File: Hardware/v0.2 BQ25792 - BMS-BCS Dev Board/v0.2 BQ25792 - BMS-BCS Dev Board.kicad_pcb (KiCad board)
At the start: 2 copper layers, 83.4 x 30 mm, 45 parts, among them J1 Barrel Jack, J2 Barrel Jack, J3 Power Out, J5 I2C Interface, Q1 ACFET1, Q2 RBFET1, Q3 ACFET2, Q4 RBFET2, Q5 BATFET, U1 BQ25792RQMR

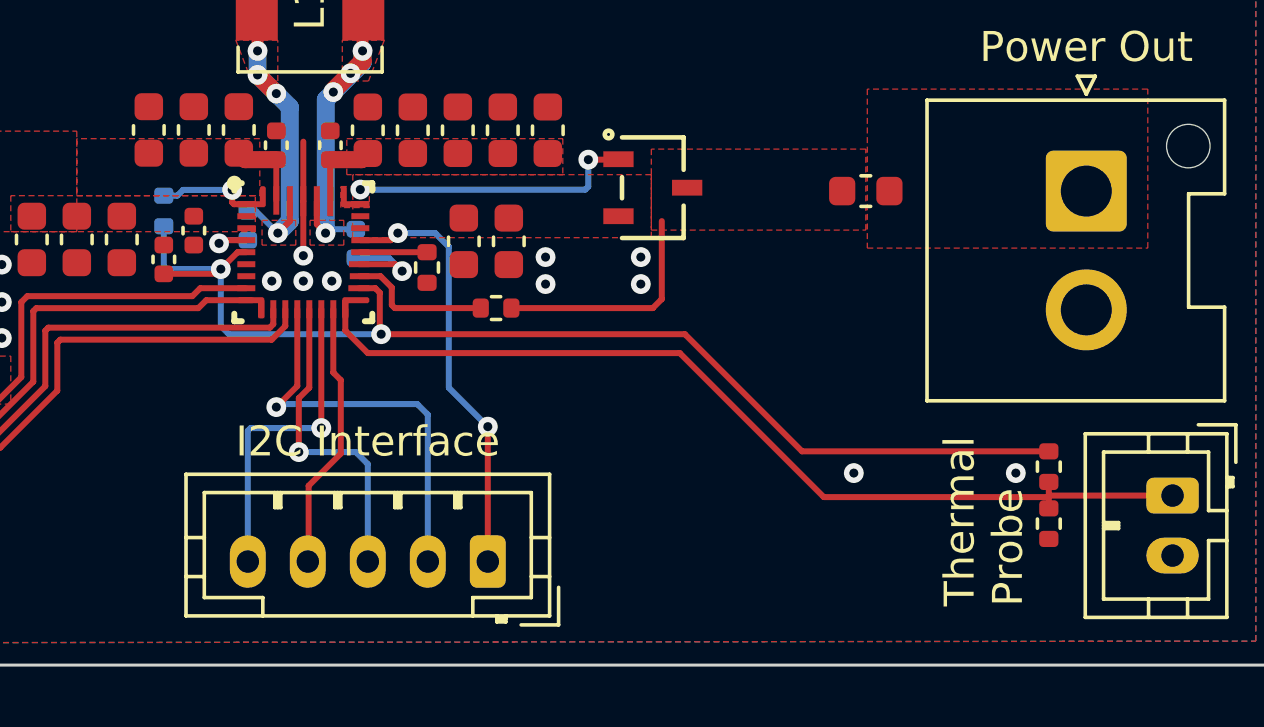
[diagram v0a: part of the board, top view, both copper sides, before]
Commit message: BMS/BCS Ordering Preparations
Finished all ordering preparations, PCB in production.
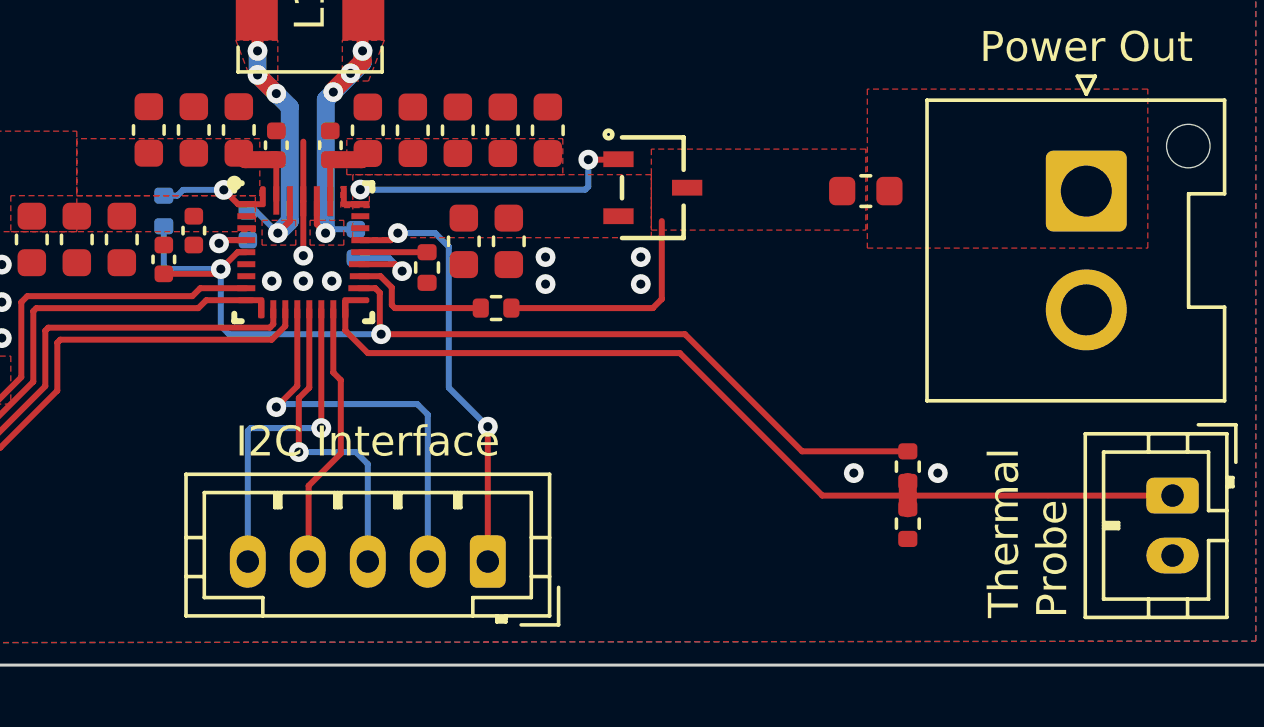
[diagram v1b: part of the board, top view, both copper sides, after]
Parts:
- moved R4 4.70 mm to (169.8, 121.8)
- moved R5 4.70 mm to (169.8, 123.7)
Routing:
- net /REGN: track 39.7 -> 35.0 mm
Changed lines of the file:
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@@
 	(footprint "Resistor_SMD:R_0402_1005Metric"
 		(layer "F.Cu")
-		(at 174.5 123.685 -90)
+		(at 169.8 123.685 -90)
 		(descr "Resistor SMD 0402 (1005 Metric), square (rectangular) end terminal, IPC_7351 nominal, (Body size source: IPC-SM-782 page 72, https://www.pcb-3d.com/wordpress/wp-content/uploads/ipc-sm-782a_amendment_1_and_2.pdf), generated with kicad-footprint-generator")
 		(tags "resistor")
@@
 	(footprint "Resistor_SMD:R_0402_1005Metric"
 		(layer "F.Cu")
-		(at 174.5 121.785 -90)
+		(at 169.8 121.785 -90)
 		(descr "Resistor SMD 0402 (1005 Metric), square (rectangular) end terminal, IPC_7351 nominal, (Body size source: IPC-SM-782 page 72, https://www.pcb-3d.com/wordpress/wp-content/uploads/ipc-sm-782a_amendment_1_and_2.pdf), generated with kicad-footprint-generator")
 		(tags "resistor")
@@
 	)
 	(gr_text "Thermal\nProbe"
-		(at 173.725 126.442858 90)
+		(at 175.2 126.831882 90)
 		(layer "F.SilkS")
 		(effects
@@
 	)
 	(via
-		(at 173.4 122)
+		(at 170.8 122)
 		(size 0.66)
 		(drill 0.3)
@@
 	)
 	(segment
-		(start 162.37 117.37)
-		(end 166.275 121.275)
+		(start 166.275 121.275)
+		(end 169.8 121.275)
 		(width 0.2)
 		(layer "F.Cu")
@@
 	)
 	(segment
-		(start 166.275 121.275)
-		(end 174.5 121.275)
+		(start 152.245478 117.37)
+		(end 162.37 117.37)
 		(width 0.2)
 		(layer "F.Cu")
@@
 	)
 	(segment
-		(start 152.049998 115.8375)
-		(end 151.499998 115.8375)
+		(start 162.37 117.37)
+		(end 166.275 121.275)
 		(width 0.2)
 		(layer "F.Cu")
@@
 	)
 	(segment
-		(start 152.2 115.987502)
-		(end 152.049998 115.8375)
+		(start 152.049998 115.8375)
+		(end 151.499998 115.8375)
 		(width 0.2)
 		(layer "F.Cu")
@@
 	)
 	(segment
-		(start 152.245478 117.37)
-		(end 162.37 117.37)
+		(start 152.2 115.987502)
+		(end 152.049998 115.8375)
 		(width 0.2)
 		(layer "F.Cu")
@@
 	)
 	(segment
-		(start 167 122.8)
-		(end 174.5 122.8)
-		(width 0.2)
-		(layer "F.Cu")
-		(net 30)
-	)
-	(segment
-		(start 162.2 118)
-		(end 167 122.8)
-		(width 0.2)
+		(start 169.8 122.295)
+		(end 169.8 122.745)
+		(width 0.6)
 		(layer "F.Cu")
 		(net 30)
 	)
 	(segment
-		(start 174.5 122.745)
-		(end 174.505 122.75)
-		(width 0.2)
+		(start 169.8 122.745)
+		(end 169.8 123.175)
+		(width 0.6)
 		(layer "F.Cu")
 		(net 30)
 	)
 	(segment
-		(start 151.049999 116.5375)
-		(end 151.049999 117.249999)
+		(start 174.505 122.75)
+		(end 178.625 122.75)
 		(width 0.2)
 		(layer "F.Cu")
@@
 	)
 	(segment
-		(start 174.5 122.295)
-		(end 174.5 122.745)
+		(start 166.945 122.75)
+		(end 174.445 122.75)
 		(width 0.2)
 		(layer "F.Cu")
@@
 	)
 	(segment
-		(start 151.049999 117.249999)
-		(end 151.8 118)
+		(start 151.049999 116.5375)
+		(end 151.049999 117.249999)
 		(width 0.2)
 		(layer "F.Cu")
@@
 	)
 	(segment
-		(start 174.5 122.745)
-		(end 174.5 123.175)
+		(start 162.2 118)
+		(end 166.945 122.745)
 		(width 0.2)
 		(layer "F.Cu")
@@
 	)
 	(segment
-		(start 174.505 122.75)
-		(end 178.625 122.75)
+		(start 151.049999 117.249999)
+		(end 151.8 118)
 		(width 0.2)
 		(layer "F.Cu")
@@
 	)
 	(segment
-		(start 147.280134 112.56047)
-		(end 147.280134 112.980134)
-		(width 0.2)
-		(layer "F.Cu")
-		(net 32)
-	)
-	(segment
-		(start 147.280134 112.980134)
-		(end 147.3375 113.0375)
+		(start 147.47703 113.0375)
+		(end 147.749999 113.0375)
 		(width 0.2)
 		(layer "F.Cu")
@@
 	)
 	(segment
-		(start 147.3375 113.0375)
-		(end 147.749999 113.0375)
+		(start 147 112.56047)
+		(end 147.47703 113.0375)
 		(width 0.2)
 		(layer "F.Cu")
@@
 	)
 	(via
-		(at 147.280134 112.56047)
+		(at 147 112.56047)
 		(size 0.66)
 		(drill 0.3)
@@
 	)
 	(segment
-		(start 145.63953 112.56047)
-		(end 145.4475 112.7525)
+		(start 147 112.56047)
+		(end 145.63953 112.56047)
 		(width 0.2)
 		(layer "B.Cu")
@@
 	)
 	(segment
-		(start 147.280134 112.56047)
-		(end 145.63953 112.56047)
+		(start 145.63953 112.56047)
+		(end 145.4475 112.7525)
 		(width 0.2)
 		(layer "B.Cu")

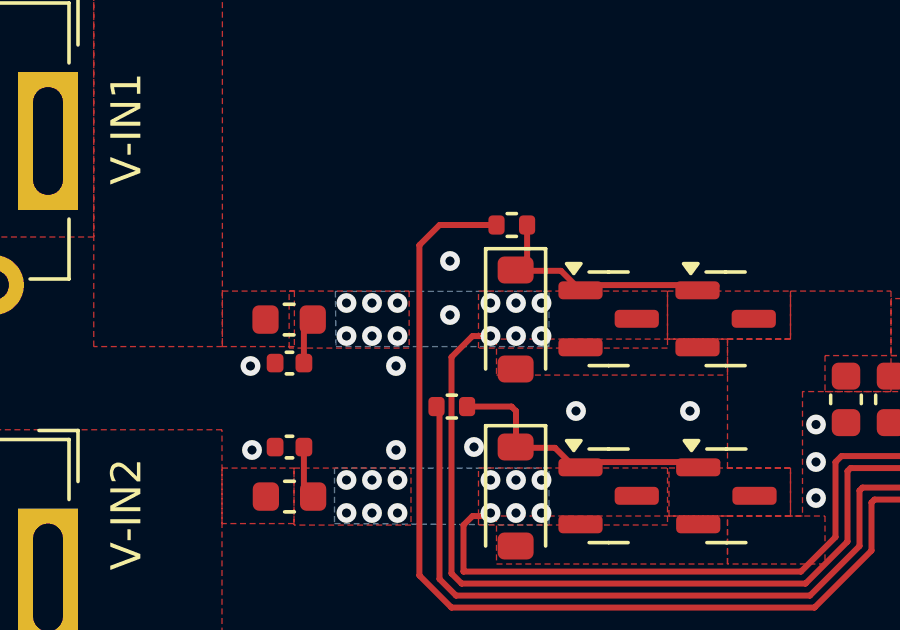
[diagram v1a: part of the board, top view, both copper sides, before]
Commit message: Production error fix
Fixed a design error post production with the high current rail. Fuck me!
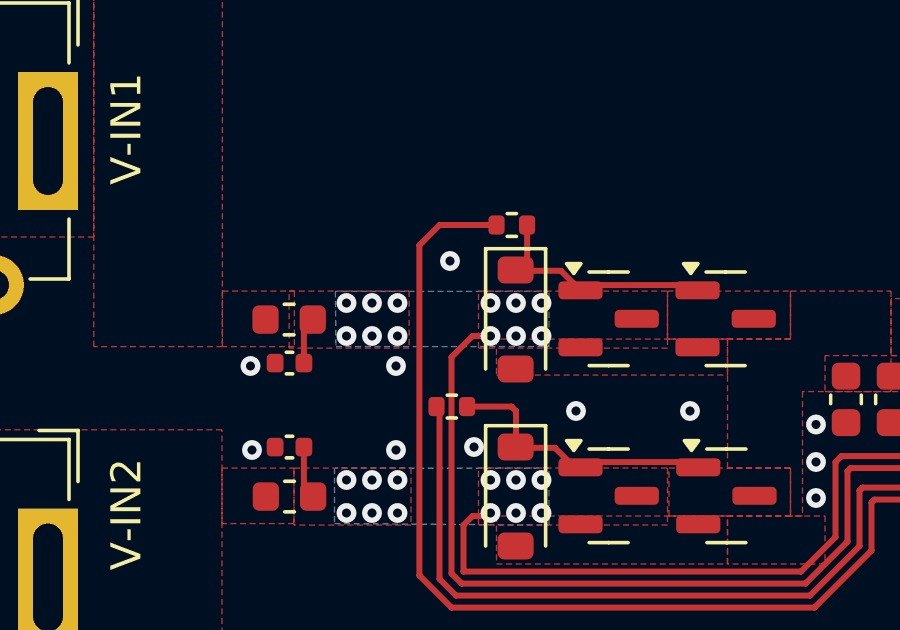
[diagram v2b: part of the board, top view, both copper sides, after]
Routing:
- net GND: vias 22 -> 21
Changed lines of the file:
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@@
-	)
-	(via
-		(at 127.4 111.4)
-		(size 0.66)
-		(drill 0.3)
-		(layers "F.Cu" "B.Cu")
-		(free yes)
-		(net 1)
 	)
 	(via

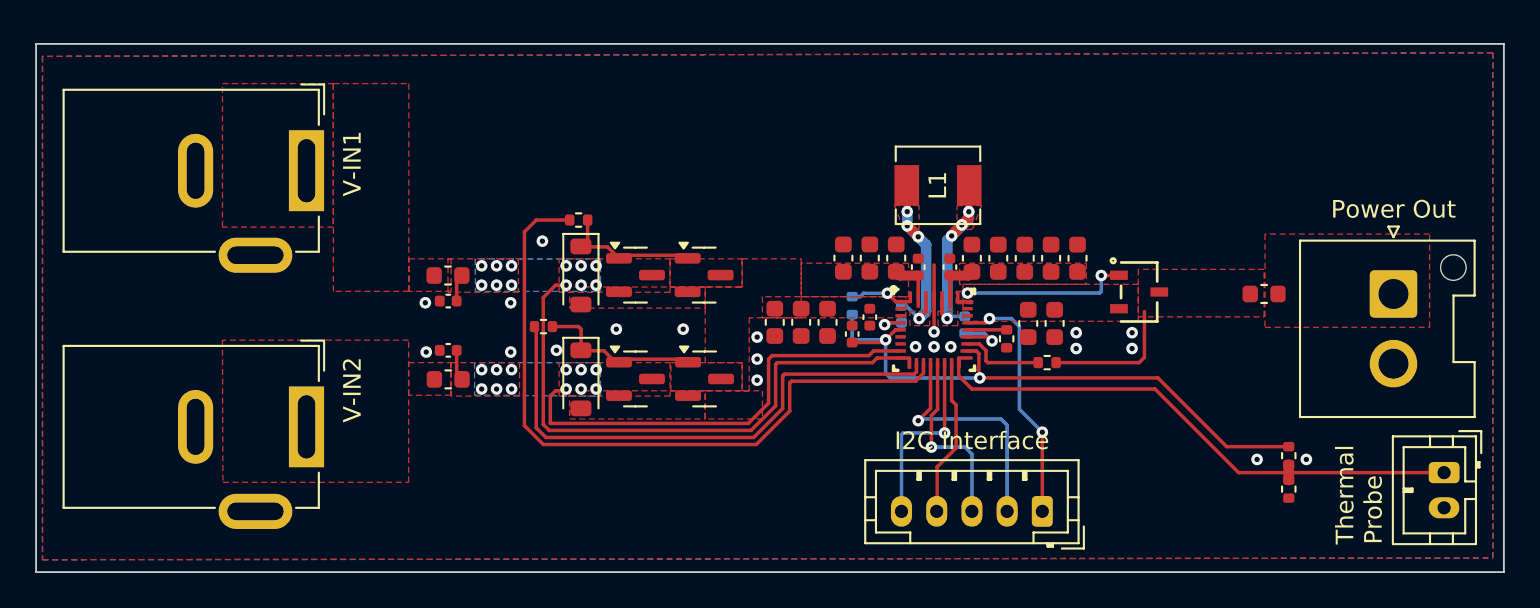
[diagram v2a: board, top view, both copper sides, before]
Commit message: BMS/BCS Board Modified
Added System Connector
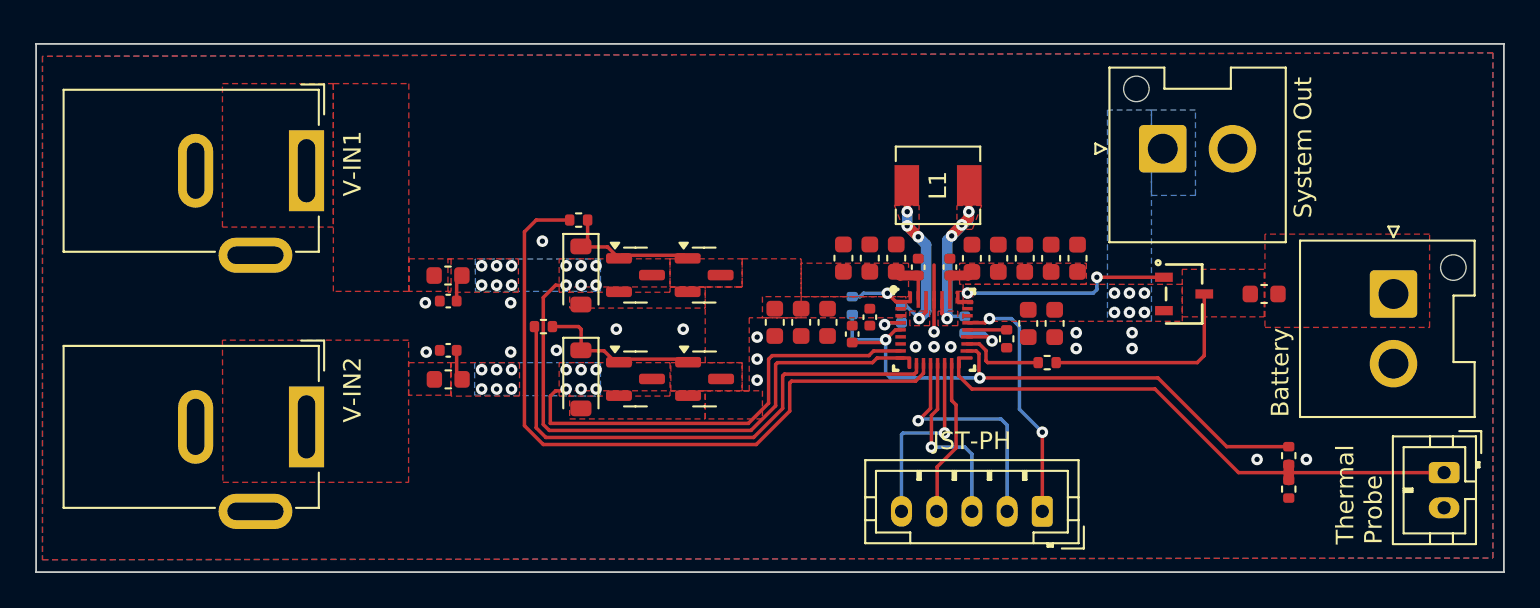
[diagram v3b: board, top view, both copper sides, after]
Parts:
- added J4: System Out, Connector_JST:JST_VH_B2P-VH-FB-B_1x02_P3.96mm_Vertical, F.Cu at (162.6, 104.3)
- J3: value Power Out -> JST-VH Shrouded
- J5: value I2C Interface -> JST-PH
- TH1: value Battery Probe -> 103AT NTC
- moved Q5 2.56 mm to (163.9, 112.6)
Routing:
- net +BATT: track 7.74 -> 12.1 mm
- net /SDRV: track 9.60 -> 12.0 mm
- net /BAT: vias 0 -> 6
- added copper zone on B.Cu, net /BAT
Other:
- board text added: "Battery"
- board text added: "System Out"
